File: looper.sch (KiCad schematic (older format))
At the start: 2 parts

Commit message: ksch: begin drawing schematics
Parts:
- removed U? (x2): WM8778, symbol WM8778
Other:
- note removed: "HIGH: I2S Mode\nLOW: 2pin Mode\nFLOAT: Hardware Mode"
- note removed: "LOW: 2 pin mode\nHIGH: I2S mode"
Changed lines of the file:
@@
 LIBS:contrib
 LIBS:valves
-LIBS:library
+LIBS:openloop
 LIBS:looper-cache
 EELAYER 25 0
@@
 $Descr A4 11693 8268
 encoding utf-8
-Sheet 1 1
+Sheet 1 3
 Title ""
 Date ""
@@
 Comment4 ""
 $EndDescr
-$Comp
-L WM8778 U?
-U 1 1 5874EDFD
-P 38850 2150
-F 0 "U?" H 38600 3600 60  0000 C CNN
-F 1 "WM8778" H 38800 3100 60  0000 C CNN
-F 2 "" H 38600 2650 60  0000 C CNN
-F 3 "" H 38600 2650 60  0000 C CNN
-	1    38850 2150
-	1    0    0    -1
-$EndComp
-Wire Wire Line
-	37450 850  37950 850
-Text Label 37450 850  0    60   ~ 0
-D_3.3V
-Wire Wire Line
-	37950 1050 37450 1050
-Text Label 37450 1050 0    60   ~ 0
-DGND
-Text Label 39750 850  0    60   ~ 0
-A_5V
-Text Label 39750 1050 0    60   ~ 0
-AGND
-Wire Wire Line
-	37950 3150 37450 3150
-Text Label 37450 3150 0    60   ~ 0
-PREAMP_OUT
-Wire Wire Line
-	37450 3450 37950 3450
-Text Label 37450 3450 0    60   ~ 0
-INST_OUT
-Wire Wire Line
-	37950 1350 37450 1350
-Text Label 37450 1350 0    60   ~ 0
-D_3.3V
-Text Notes 36700 1350 0    60   ~ 0
-LOW: 2 pin mode\nHIGH: I2S mode
-$Comp
-L WM8778 U?
-U 1 1 587609C5
-P 3200 3050
-F 0 "U?" H 2950 4500 60  0000 C CNN
-F 1 "WM8778" H 3150 4000 60  0000 C CNN
-F 2 "" H 2950 3550 60  0000 C CNN
-F 3 "" H 2950 3550 60  0000 C CNN
-	1    3200 3050
-	1    0    0    -1
-$EndComp
-Wire Wire Line
-	2300 1750 2000 1750
-Text Label 2000 1750 0    60   ~ 0
-D_3.3V
-Wire Wire Line
-	2300 1950 2000 1950
-Text Label 2000 1950 0    60   ~ 0
-DGND
-Wire Wire Line
-	2300 2250 2000 2250
-Text Label 2000 2250 0    60   ~ 0
-D_3.3V
-Text Notes 1050 2350 0    60   ~ 0
-HIGH: I2S Mode\nLOW: 2pin Mode\nFLOAT: Hardware Mode
-Wire Wire Line
-	2300 2400 2050 2400
-Text Label 2050 2400 0    60   ~ 0
-CE
-Wire Wire Line
-	2300 2500 2050 2500
-Text Label 2050 2500 0    60   ~ 0
-DI
-Wire Wire Line
-	2300 2600 2050 2600
-Text Label 2050 2600 0    60   ~ 0
-CL
-Wire Wire Line
-	4100 1750 4350 1750
-Text Label 4350 1750 2    60   ~ 0
-A_5V
-Wire Wire Line
-	4100 1950 4350 1950
-Wire Wire Line
-	4350 1950 4350 1950
-Text Label 4350 1950 2    60   ~ 0
-AGND
+$Sheet
+S 2600 2950 1050 850
+U 58B347F0
+F0 "Codec" 60
+F1 "codec.sch" 60
+F2 "3.3V" I L 2600 3050 60
+F3 "DGND" I L 2600 3200 60
+F4 "5V" I L 2600 3350 60
+F5 "AGND" I L 2600 3500 60
+$EndSheet
+$Sheet
+S 2150 1850 1350 750
+U 58B3513F
+F0 "power schematic" 60
+F1 "power.sch" 60
+$EndSheet
 $EndSCHEMATC

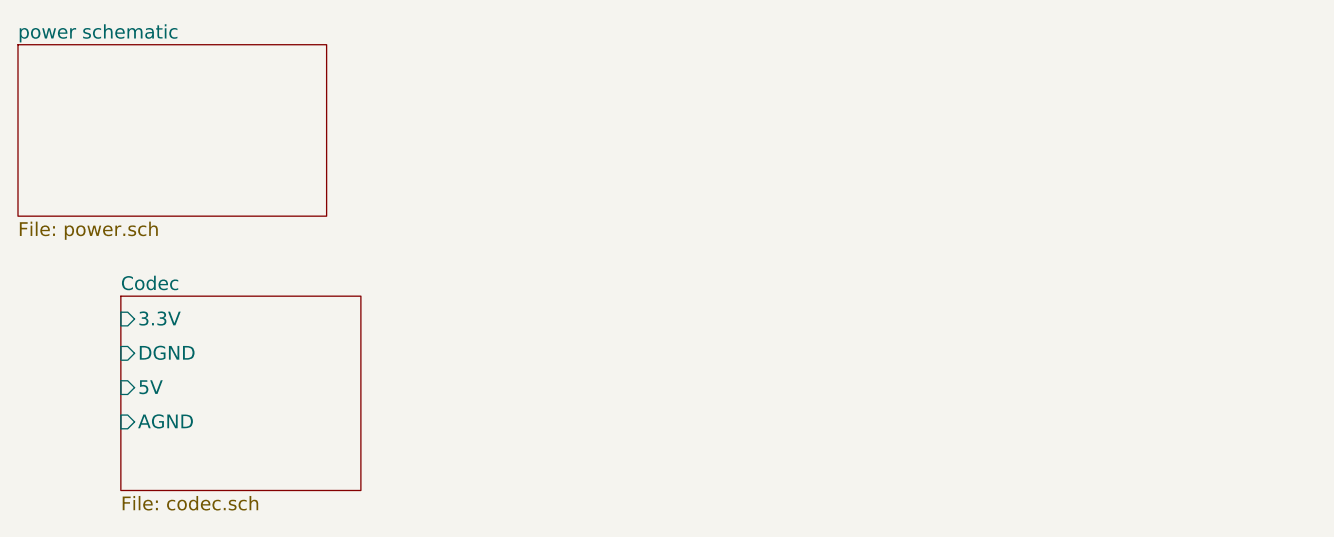
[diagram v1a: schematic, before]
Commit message: ksch: add uC power and programming pins
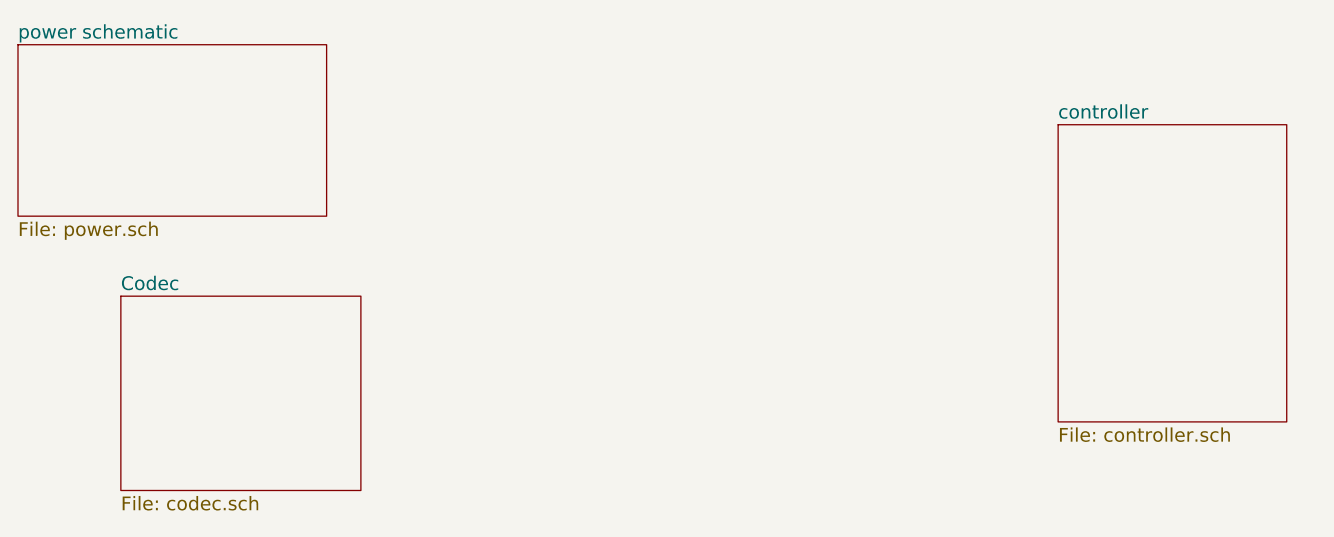
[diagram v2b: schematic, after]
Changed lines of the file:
@@
 EESchema Schematic File Version 2
+LIBS:openloop
+LIBS:74xgxx
+LIBS:74xx
+LIBS:ac-dc
+LIBS:actel
+LIBS:adc-dac
+LIBS:allegro
+LIBS:Altera
+LIBS:analog_devices
+LIBS:analog_switches
+LIBS:atmel
+LIBS:audio
+LIBS:battery_management
+LIBS:bbd
+LIBS:bosch
+LIBS:brooktre
+LIBS:cmos_ieee
+LIBS:cmos4000
+LIBS:conn
+LIBS:contrib
+LIBS:cypress
+LIBS:dc-dc
+LIBS:device
+LIBS:digital-audio
+LIBS:diode
+LIBS:display
+LIBS:dsp
+LIBS:elec-unifil
+LIBS:ESD_Protection
+LIBS:ftdi
+LIBS:gennum
+LIBS:graphic
+LIBS:hc11
+LIBS:intel
+LIBS:interface
+LIBS:intersil
+LIBS:ir
+LIBS:Lattice
+LIBS:leds
+LIBS:linear
+LIBS:logo
+LIBS:maxim
+LIBS:mechanical
+LIBS:memory
+LIBS:microchip
+LIBS:microchip_dspic33dsc
+LIBS:microchip_pic10mcu
+LIBS:microchip_pic12mcu
+LIBS:microchip_pic16mcu
+LIBS:microchip_pic18mcu
+LIBS:microchip_pic24mcu
+LIBS:microchip_pic32mcu
+LIBS:microcontrollers
+LIBS:modules
+LIBS:motor_drivers
+LIBS:motorola
+LIBS:motors
+LIBS:msp430
+LIBS:nordicsemi
+LIBS:nxp
+LIBS:nxp_armmcu
+LIBS:onsemi
+LIBS:opto
+LIBS:Oscillators
+LIBS:philips
 LIBS:power
-LIBS:device
+LIBS:Power_Management
+LIBS:powerint
+LIBS:pspice
+LIBS:references
+LIBS:regul
+LIBS:relays
+LIBS:rfcom
+LIBS:sensors
+LIBS:silabs
+LIBS:siliconi
+LIBS:stm8
+LIBS:stm32
+LIBS:supertex
+LIBS:switches
+LIBS:texas
+LIBS:transf
 LIBS:transistors
-LIBS:conn
-LIBS:linear
-LIBS:regul
-LIBS:74xx
-LIBS:cmos4000
-LIBS:adc-dac
-LIBS:memory
+LIBS:triac_thyristor
+LIBS:ttl_ieee
+LIBS:valves
+LIBS:video
+LIBS:wiznet
+LIBS:Worldsemi
+LIBS:Xicor
 LIBS:xilinx
-LIBS:microcontrollers
-LIBS:dsp
-LIBS:microchip
-LIBS:analog_switches
-LIBS:motorola
-LIBS:texas
-LIBS:intel
-LIBS:audio
-LIBS:interface
-LIBS:digital-audio
-LIBS:philips
-LIBS:display
-LIBS:cypress
-LIBS:siliconi
-LIBS:opto
-LIBS:atmel
-LIBS:contrib
-LIBS:valves
-LIBS:openloop
-LIBS:looper-cache
+LIBS:zetex
+LIBS:Zilog
 EELAYER 25 0
 EELAYER END
 $Descr A4 11693 8268
 encoding utf-8
-Sheet 1 3
+Sheet 1 4
 Title ""
 Date ""
@@
 $EndDescr
 $Sheet
-S 2600 2950 1050 850
-U 58B347F0
-F0 "Codec" 60
-F1 "codec.sch" 60
-F2 "3.3V" I L 2600 3050 60
-F3 "DGND" I L 2600 3200 60
-F4 "5V" I L 2600 3350 60
-F5 "AGND" I L 2600 3500 60
-$EndSheet
-$Sheet
 S 2150 1850 1350 750
 U 58B3513F
@@
 F1 "power.sch" 60
 $EndSheet
+$Sheet
+S 6700 2200 1000 1300
+U 58D0F874
+F0 "controller" 60
+F1 "controller.sch" 60
+$EndSheet
+$Sheet
+S 2600 2950 1050 850
+U 58B347F0
+F0 "Codec" 60
+F1 "codec.sch" 60
+$EndSheet
 $EndSCHEMATC
